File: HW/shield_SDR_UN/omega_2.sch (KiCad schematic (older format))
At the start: 17 parts

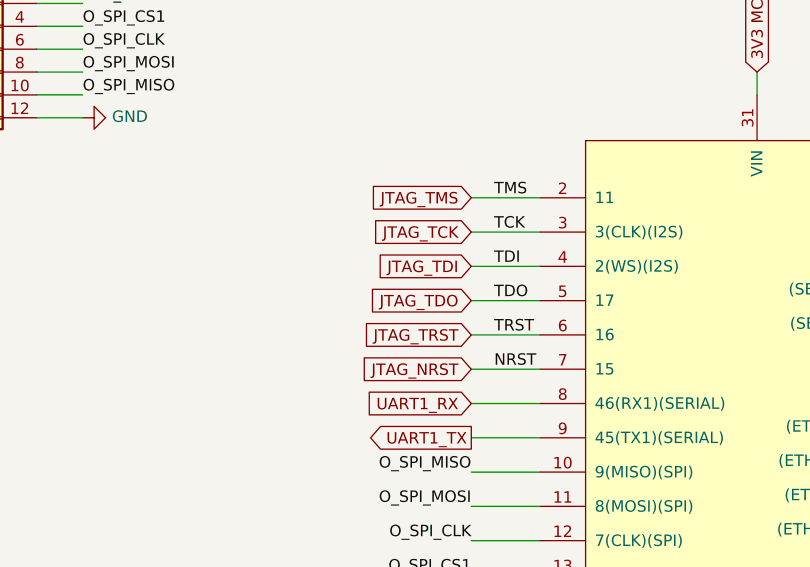
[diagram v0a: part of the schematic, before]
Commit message: JTAG routed
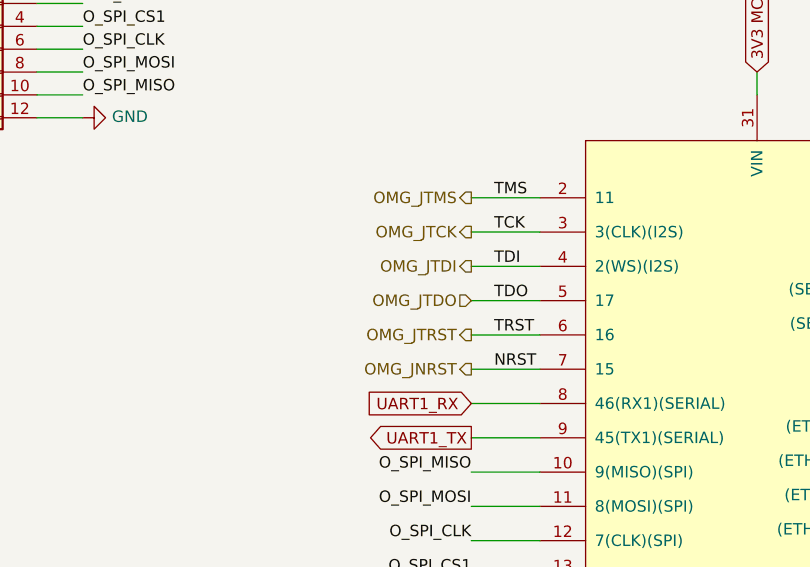
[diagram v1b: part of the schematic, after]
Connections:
- net JTAG_NRST renamed OMG_JNRST
- net JTAG_TCK renamed OMG_JTCK
- net JTAG_TDI renamed OMG_JTDI
- net JTAG_TDO renamed OMG_JTDO
- net JTAG_TMS renamed OMG_JTMS
- net JTAG_TRST renamed OMG_JTRST
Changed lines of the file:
@@
 Text Label 5650 2700 0    50   ~ 0
 NRST
-Text GLabel 5550 1950 0    50   Input ~ 0
-JTAG_TMS
-Text GLabel 5550 2100 0    50   Input ~ 0
-JTAG_TCK
-Text GLabel 5550 2250 0    50   Input ~ 0
-JTAG_TDI
-Text GLabel 5550 2400 0    50   Input ~ 0
-JTAG_TDO
-Text GLabel 5550 2550 0    50   Input ~ 0
-JTAG_TRST
-Text GLabel 5550 2700 0    50   Input ~ 0
-JTAG_NRST
 Wire Wire Line
 	7750 3850 8200 3850
@@
 Wire Wire Line
 	2450 5900 2450 5800
+Text HLabel 5550 1950 0    50   Output ~ 0
+OMG_JTMS
+Text HLabel 5550 2100 0    50   Output ~ 0
+OMG_JTCK
+Text HLabel 5550 2250 0    50   Output ~ 0
+OMG_JTDI
+Text HLabel 5550 2550 0    50   Output ~ 0
+OMG_JTRST
+Text HLabel 5550 2700 0    50   Output ~ 0
+OMG_JNRST
+Text HLabel 5550 2400 0    50   Input ~ 0
+OMG_JTDO
 $EndSCHEMATC

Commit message: Schematic finished
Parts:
- removed FB? (x2): FILTER, symbol hackrf-one-packages:FILTER
- removed SW?: SW_Push, SWITCH_FSM1LPA, symbol FSM1LPTR:FSM1LPTR
- added FB2: SRF2012-900YA, lib:SRF2012-900YA, symbol SRF2012900YA:SRF2012-900YA
- added S5: TL1014BF160QG, lib:TL1014BF160QG, symbol TL1014BF160QG:TL1014BF160QG
- D10: renamed from D?; footprint (none) -> Diode_SMD:D_SMA_Handsoldering; Digikey (none) -> SMAZ5V1-FDICT-ND
- D11: renamed from D?; footprint Package_TO_SOT_SMD:SOT-23 -> Package_TO_SOT_SMD:SOT-23_Handsoldering; Digikey (none) -> F2714CT-ND
- L3: renamed from L?; footprint (none) -> Inductor_SMD:L_0603_1608Metric_Pad1.05x0.95mm_HandSolder; Digikey (none) -> 732-1593-1-ND; digikey 732-1593-1-ND -> (none)
- gave numbers to parts that had none: 11
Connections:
- net GND: now also S5.3, S5.4
- net RST_BTN: now also S5.1, S5.2
- net USB_D+: now also FB2.4
- net USB_D-: now also FB2.1
- net at D11.1 (K), J5.2 (D-): now also FB2.2
- net at D11.2 (K), J5.3 (D+): now also FB2.3

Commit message: organizacion PCB
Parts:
- C122: footprint Capacitor_SMD:C_0402_1005Metric -> Capacitor_SMD:C_0603_1608Metric_Pad1.05x0.95mm_HandSolder
- J6: footprint (none) -> Connector_PinHeader_2.54mm:PinHeader_2x06_P2.54mm_Vertical
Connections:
- net 3v3 MCU is gone; now on net 3V3 MCU: R62.1
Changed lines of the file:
@@
 F 0 "C122" H 1565 1396 50  0000 L CNN
 F 1 "1uF" H 1565 1205 50  0000 L CNN
-F 2 "Capacitor_SMD:C_0402_1005Metric" H 1538 1150 50  0001 C CNN
+F 2 "Capacitor_SMD:C_0603_1608Metric_Pad1.05x0.95mm_HandSolder" H 1538 1150 50  0001 C CNN
 F 3 "http://www.samsungsem.com/kr/support/product-search/mlcc/__icsFiles/afieldfile/2019/05/10/19-CL10A105KP8NNNC.pdf" H 1500 1300 50  0001 C CNN
 F 4 "1276-1182-1-ND" H 1500 1300 50  0001 C CNN "Digikey"
@@
 F 0 "J6" H 3400 1717 50  0000 C CNN
 F 1 "Conn_02x06_Odd_Even" H 3400 1626 50  0000 C CNN
-F 2 "" H 3350 1300 50  0001 C CNN
+F 2 "Connector_PinHeader_2.54mm:PinHeader_2x06_P2.54mm_Vertical" H 3350 1300 50  0001 C CNN
 F 3 "~" H 3350 1300 50  0001 C CNN
 	1    3350 1300
@@
 Text Label 3850 1300 0    50   ~ 0
 O_SPI_CLK
-Text GLabel 1000 5300 0    50   Input ~ 0
-3v3 MCU
 $Comp
 L Device:R R62
@@
 Wire Wire Line
 	1750 6250 1750 6450
+Text GLabel 1000 5300 0    50   Input ~ 0
+3V3 MCU
 $EndSCHEMATC

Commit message: Omega 2 PCB
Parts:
- D10: footprint Diode_SMD:D_SMA_Handsoldering -> Diode_SMD:D_SOD-123; Digikey SMAZ5V1-FDICT-ND -> MMSZ5231BT1GOSCT-ND
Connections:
- net I2C_SCL: now also J6.8 (Pin_8); no longer J6.3 (Pin_3)
- net I2C_SDA: now also J6.7 (Pin_7); no longer J6.5 (Pin_5)
- net O_SPI_CLK: now also J6.4 (Pin_4); no longer J6.6 (Pin_6)
- net O_SPI_CS1: now also J6.3 (Pin_3); no longer J6.4 (Pin_4)
- net O_SPI_MISO: now also J6.6 (Pin_6); no longer J6.10 (Pin_10)
- net O_SPI_MOSI: now also J6.5 (Pin_5); no longer J6.8 (Pin_8)
- net SER_RX0: now also J6.9 (Pin_9); no longer J6.7 (Pin_7)
- net SER_TX0: now also J6.10 (Pin_10); no longer J6.9 (Pin_9)
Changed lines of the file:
@@
 F 0 "D10" V 1504 4279 50  0000 L CNN
 F 1 "D_Zener-5.1V-1W" V 1650 3450 50  0000 L CNN
-F 2 "Diode_SMD:D_SMA_Handsoldering" H 1550 4200 50  0001 C CNN
-F 3 "https://www.diodes.com/assets/Datasheets/ds18015.pdf" H 1550 4200 50  0001 C CNN
-F 4 " SMAZ5V1-FDICT-ND" V 1550 4200 50  0001 C CNN "Digikey"
+F 2 "Diode_SMD:D_SOD-123" H 1550 4200 50  0001 C CNN
+F 3 "http://www.onsemi.com/pub/Collateral/MMSZ5221BT1-D.PDF" H 1550 4200 50  0001 C CNN
+F 4 "MMSZ5231BT1GOSCT-ND" V 1550 4200 50  0001 C CNN "Digikey"
 	1    1550 4200
 	0    1    1    0
@@
 	0    1    1    0
 $EndComp
+Text Label 2950 1500 2    50   ~ 0
+SER_RX0
 Text Label 2950 1400 2    50   ~ 0
-SER_RX0
-Text Label 2950 1500 2    50   ~ 0
-SER_TX0
-Text Label 2950 1300 2    50   ~ 0
 I2C_SDA
-Text Label 2950 1200 2    50   ~ 0
+Text Label 3850 1400 0    50   ~ 0
 I2C_SCL
 Text Label 2950 1100 2    50   ~ 0
@@
 	0    -1   -1   0
 $EndComp
-Text Label 3850 1500 0    50   ~ 0
+Text Label 3850 1300 0    50   ~ 0
 O_SPI_MISO
-Text Label 3850 1400 0    50   ~ 0
+Text Label 2950 1300 2    50   ~ 0
 O_SPI_MOSI
+Text Label 2950 1200 2    50   ~ 0
+O_SPI_CS1
 Text Label 3850 1200 0    50   ~ 0
-O_SPI_CS1
-Text Label 3850 1300 0    50   ~ 0
 O_SPI_CLK
 $Comp
@@
 Text GLabel 1000 5300 0    50   Input ~ 0
 3V3 MCU
+Text Label 3850 1500 0    50   ~ 0
+SER_TX0
 $EndSCHEMATC

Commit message: PCB route V1
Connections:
- net 3V3 MCU: now also J6.1 (Pin_1), J6.2 (Pin_2)
- net 3V3_OMEG: no longer J6.1 (Pin_1), J6.2 (Pin_2)
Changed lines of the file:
@@
 	3150 1600 2950 1600
-Wire Wire Line
-	3150 1100 2950 1100
 Wire Wire Line
 	7750 2800 7950 2800
@@
 Text Label 3850 1400 0    50   ~ 0
 I2C_SCL
-Text Label 2950 1100 2    50   ~ 0
-3V3_OMEG
 Text Notes 2600 750  0    50   ~ 0
 Omega 2 Pinout
@@
 $EndComp
 Wire Wire Line
-	3650 1100 3850 1100
-Wire Wire Line
 	3650 1200 3850 1200
 Wire Wire Line
@@
 Wire Wire Line
 	3650 1600 3850 1600
-Text Label 3850 1100 0    50   ~ 0
-3V3_OMEG
 $Comp
 L power:GND #PWR0152
@@
 Text Label 3850 1500 0    50   ~ 0
 SER_TX0
+Text GLabel 2550 1100 0    50   Input ~ 0
+3V3 MCU
+Text GLabel 4225 1100 2    50   Input ~ 0
+3V3 MCU
+Wire Wire Line
+	3650 1100 4225 1100
+Wire Wire Line
+	2550 1100 3150 1100
 $EndSCHEMATC

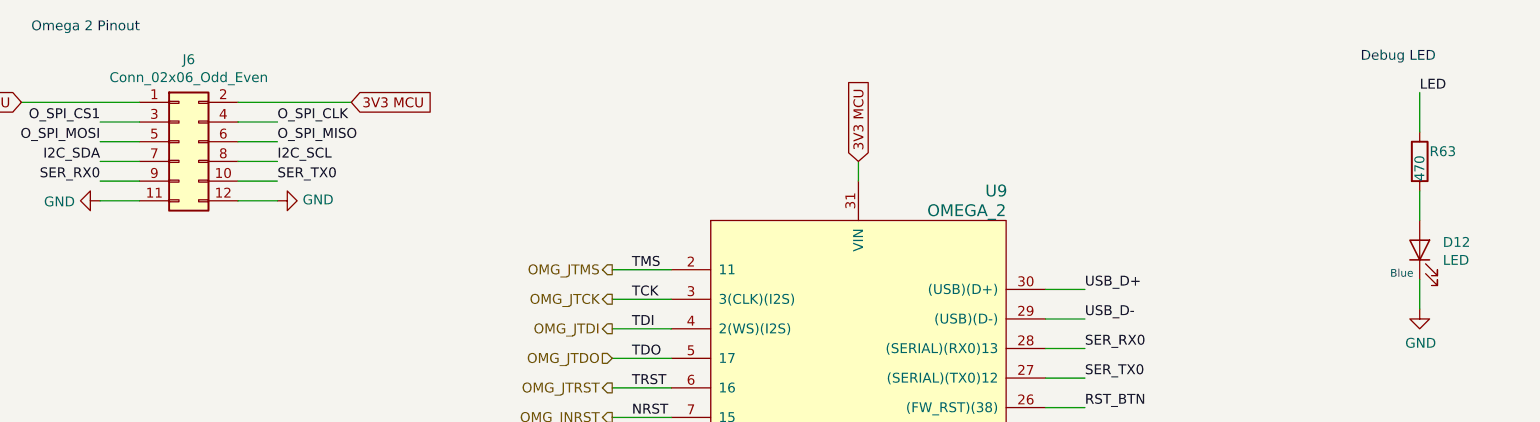
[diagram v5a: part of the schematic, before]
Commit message: Partnumbers modified
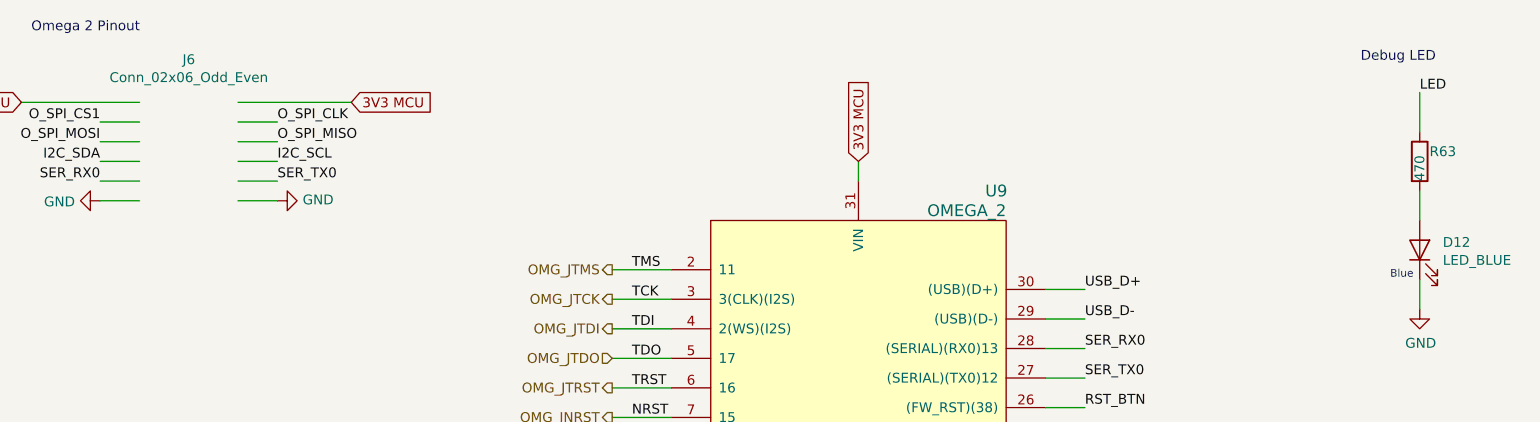
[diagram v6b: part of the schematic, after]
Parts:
- D12: value LED -> LED_BLUE
- J6: Digikey (none) -> 609-3219-ND
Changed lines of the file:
@@
 AR Path="/5CFB52DC/5D35F1A3" Ref="D12"  Part="1"
 F 0 "D12" V 9689 1733 50  0000 R CNN
-F 1 "LED" V 9598 1733 50  0000 R CNN
+F 1 "LED_BLUE" V 9598 1733 50  0000 R CNN
 F 2 "LED_SMD:LED_0805_2012Metric_Pad1.15x1.40mm_HandSolder" H 9650 1850 50  0001 C CNN
 F 3 "http://optoelectronics.liteon.com/upload/download/DS22-2000-239/LTST-S220TBKT.pdf" H 9650 1850 50  0001 C CNN
@@
 $Comp
 L Connector_Generic:Conn_02x06_Odd_Even J6
-U 1 1 5CE675B7
+U 0 0 5CE675B7
 P 3350 1300
 F 0 "J6" H 3400 1717 50  0000 C CNN
@@
 F 2 "Connector_PinHeader_2.54mm:PinHeader_2x06_P2.54mm_Vertical" H 3350 1300 50  0001 C CNN
 F 3 "~" H 3350 1300 50  0001 C CNN
-	1    3350 1300
+F 4 "609-3219-ND" H 3350 1300 50  0001 C CNN "Digikey"
+	0    3350 1300
 	1    0    0    -1
 $EndComp
